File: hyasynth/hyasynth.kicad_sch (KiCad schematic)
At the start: 45 parts, among them J1 Conn_01x04_Male, J2 Conn_01x03_Male, J3 Conn_01x09_Male, J4 Conn_01x05_Male, J5 Conn_01x02_Male, SW1 Power Switch, SW10 G# Ab, SW11 A, SW12 A# Bb, SW13 B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

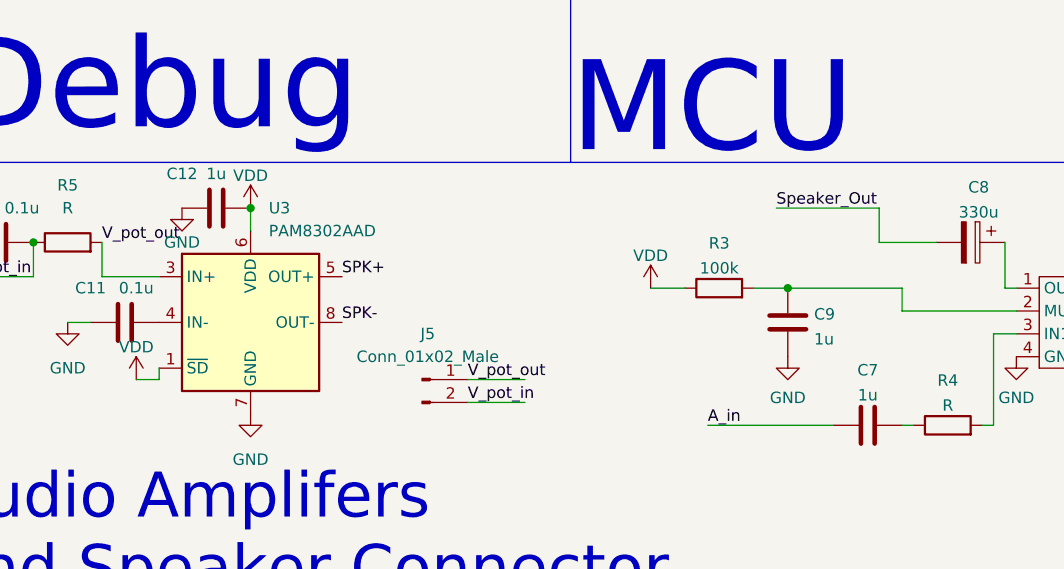
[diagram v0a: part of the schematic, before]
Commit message: set battery positions, adjusted for caps
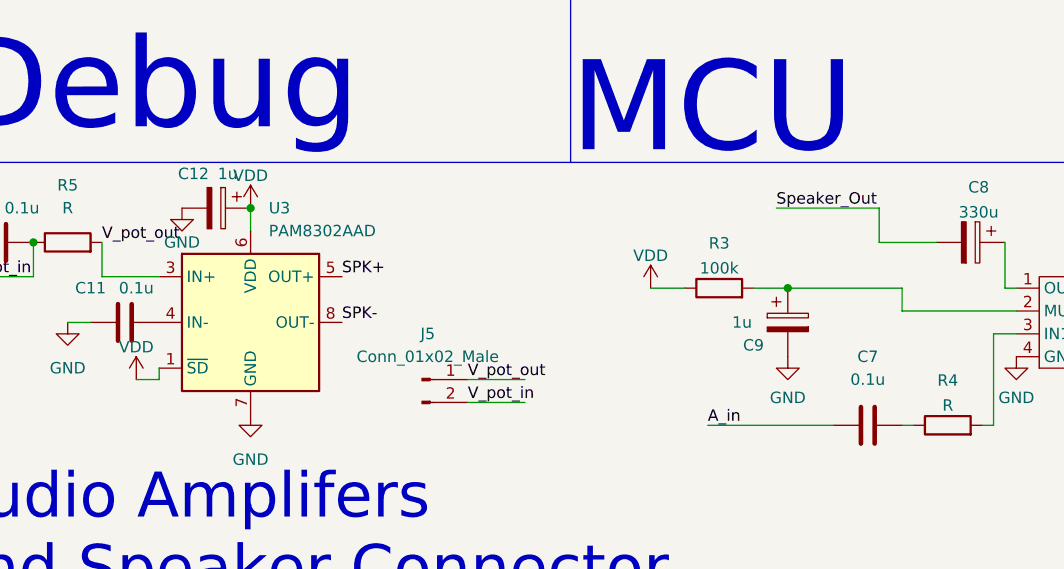
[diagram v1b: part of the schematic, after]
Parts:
- removed C12, C9: 1u, Capacitor_Tantalum_SMD:CP_EIA-3528-21_Kemet-B_Pad1.50x2.35mm_HandSolder, symbol Device:C
- added C12, C9: 1u, Capacitor_Tantalum_SMD:CP_EIA-3528-12_Kemet-T_Pad1.50x2.35mm_HandSolder, symbol Device:C_Polarized
- C7: value 1u -> 0.1u; footprint Capacitor_Tantalum_SMD:CP_EIA-3528-21_Kemet-B_Pad1.50x2.35mm_HandSolder -> Capacitor_SMD:C_0805_2012Metric_Pad1.18x1.45mm_HandSolder
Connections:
- net GND: now also C12.2, C9.2
- net VDD: now also C12.1
- net at R3.2, U2.2 (MUTE): now also C9.1
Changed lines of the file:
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@@
   (junction (at 38.1 175.26) (diameter 0) (color 0 0 0 0)
   )
+  (junction (at 175.26 97.79) (diameter 0) (color 0 0 0 0)
+  )
   (junction (at 267.97 158.75) (diameter 0) (color 0 0 0 0)
   )
+  (junction (at 212.09 49.53) (diameter 0) (color 0 0 0 0)
+  )
+  (junction (at 181.61 40.64) (diameter 0) (color 0 0 0 0)
+  )
+  (junction (at 181.61 36.83) (diameter 0) (color 0 0 0 0)
+  )
+  (junction (at 123.19 36.83) (diameter 0) (color 0 0 0 0)
+  )
+  (junction (at 86.36 185.42) (diameter 0) (color 0 0 0 0)
+  )
+  (junction (at 252.73 158.75) (diameter 0) (color 0 0 0 0)
+  )
+  (junction (at 215.9 44.45) (diameter 0) (color 0 0 0 0)
+  )
+  (junction (at 101.6 175.26) (diameter 0) (color 0 0 0 0)
+  )
+  (junction (at 158.75 40.64) (diameter 0) (color 0 0 0 0)
+  )
+  (junction (at 132.08 185.42) (diameter 0) (color 0 0 0 0)
+  )
+  (junction (at 158.75 29.21) (diameter 0) (color 0 0 0 0)
+  )
+  (junction (at 158.75 48.26) (diameter 0) (color 0 0 0 0)
+  )
+  (junction (at 69.85 175.26) (diameter 0) (color 0 0 0 0)
+  )
+  (junction (at 238.76 97.79) (diameter 0) (color 0 0 0 0)
+  )
+  (junction (at 91.44 92.71) (diameter 0) (color 0 0 0 0)
+  )
+  (junction (at 21.59 175.26) (diameter 0) (color 0 0 0 0)
+  )
+  (junction (at 215.9 49.53) (diameter 0) (color 0 0 0 0)
+  )
+  (junction (at 181.61 48.26) (diameter 0) (color 0 0 0 0)
+  )
+  (junction (at 101.6 185.42) (diameter 0) (color 0 0 0 0)
+  )
+  (junction (at 116.84 185.42) (diameter 0) (color 0 0 0 0)
+  )
+  (junction (at 54.61 185.42) (diameter 0) (color 0 0 0 0)
+  )
+  (junction (at 38.1 185.42) (diameter 0) (color 0 0 0 0)
+  )
+  (junction (at 86.36 175.26) (diameter 0) (color 0 0 0 0)
+  )
   (junction (at 115.57 88.9) (diameter 0) (color 0 0 0 0)
-  )
-  (junction (at 212.09 49.53) (diameter 0) (color 0 0 0 0)
-  )
-  (junction (at 181.61 40.64) (diameter 0) (color 0 0 0 0)
-  )
-  (junction (at 181.61 36.83) (diameter 0) (color 0 0 0 0)
-  )
-  (junction (at 123.19 36.83) (diameter 0) (color 0 0 0 0)
-  )
-  (junction (at 86.36 185.42) (diameter 0) (color 0 0 0 0)
-  )
-  (junction (at 252.73 158.75) (diameter 0) (color 0 0 0 0)
-  )
-  (junction (at 215.9 44.45) (diameter 0) (color 0 0 0 0)
-  )
-  (junction (at 101.6 175.26) (diameter 0) (color 0 0 0 0)
-  )
-  (junction (at 158.75 40.64) (diameter 0) (color 0 0 0 0)
-  )
-  (junction (at 132.08 185.42) (diameter 0) (color 0 0 0 0)
-  )
-  (junction (at 158.75 29.21) (diameter 0) (color 0 0 0 0)
-  )
-  (junction (at 158.75 48.26) (diameter 0) (color 0 0 0 0)
-  )
-  (junction (at 69.85 175.26) (diameter 0) (color 0 0 0 0)
-  )
-  (junction (at 238.76 97.79) (diameter 0) (color 0 0 0 0)
-  )
-  (junction (at 91.44 92.71) (diameter 0) (color 0 0 0 0)
-  )
-  (junction (at 21.59 175.26) (diameter 0) (color 0 0 0 0)
-  )
-  (junction (at 215.9 49.53) (diameter 0) (color 0 0 0 0)
-  )
-  (junction (at 181.61 48.26) (diameter 0) (color 0 0 0 0)
-  )
-  (junction (at 101.6 185.42) (diameter 0) (color 0 0 0 0)
-  )
-  (junction (at 175.26 97.79) (diameter 0) (color 0 0 0 0)
-  )
-  (junction (at 116.84 185.42) (diameter 0) (color 0 0 0 0)
-  )
-  (junction (at 54.61 185.42) (diameter 0) (color 0 0 0 0)
-  )
-  (junction (at 38.1 185.42) (diameter 0) (color 0 0 0 0)
-  )
-  (junction (at 86.36 175.26) (diameter 0) (color 0 0 0 0)
   )
   (no_connect (at 224.79 105.41))
@@
     (stroke (width 0) (type default) (color 0 0 0 0))
   )
-  (wire (pts (xy 187.96 97.79) (xy 175.26 97.79))
-    (stroke (width 0) (type default) (color 0 0 0 0))
-  )
   (wire (pts (xy 105.41 106.68) (xy 105.41 107.95))
     (stroke (width 0) (type default) (color 0 0 0 0))
@@
   )
   (wire (pts (xy 252.73 152.4) (xy 252.73 158.75))
+    (stroke (width 0) (type default) (color 0 0 0 0))
+  )
+  (wire (pts (xy 175.26 97.79) (xy 187.96 97.79))
     (stroke (width 0) (type default) (color 0 0 0 0))
   )
@@
     (pin "2")
   )
-  (symbol (lib_id "Device:C") (at 175.26 101.6 0) (unit 1)
-    (in_bom yes) (on_board yes) (fields_autoplaced)
-    (property "Reference" "C9" (id 0) (at 178.181 100.6915 0)
-      (effects (font (size 1.27 1.27)) (justify left))
-    )
-    (property "Value" "1u" (id 1) (at 178.181 103.4666 0)
-      (effects (font (size 1.27 1.27)) (justify left))
-    )
-    (property "Footprint" "Capacitor_Tantalum_SMD:CP_EIA-3528-21_Kemet-B_Pad1.50x2.35mm_HandSolder" (id 2) (at 176.2252 105.41 0)
-      (effects (font (size 1.27 1.27)) hide)
-    )
-    (property "Datasheet" "~" (id 3) (at 175.26 101.6 0)
-      (effects (font (size 1.27 1.27)) hide)
-    )
-    (pin "1")
-    (pin "2")
-  )
   (symbol (lib_id "power:VDD") (at 160.02 97.79 0) (unit 1)
     (in_bom yes) (on_board yes) (fields_autoplaced)
@@
     (pin "2")
   )
-  (symbol (lib_id "Device:C") (at 111.76 88.9 90) (unit 1)
-    (in_bom yes) (on_board yes)
-    (property "Reference" "C12" (id 0) (at 107.95 85.09 90))
-    (property "Value" "1u" (id 1) (at 111.76 85.09 90))
-    (property "Footprint" "Capacitor_Tantalum_SMD:CP_EIA-3528-21_Kemet-B_Pad1.50x2.35mm_HandSolder" (id 2) (at 115.57 87.9348 0)
-      (effects (font (size 1.27 1.27)) hide)
-    )
-    (property "Datasheet" "~" (id 3) (at 111.76 88.9 0)
-      (effects (font (size 1.27 1.27)) hide)
-    )
-    (pin "1")
-    (pin "2")
-  )
   (symbol (lib_id "power:GND") (at 31.75 57.15 0) (unit 1)
     (in_bom yes) (on_board yes)
@@
     )
     (property "Datasheet" "~" (id 3) (at 257.81 147.32 0)
+      (effects (font (size 1.27 1.27)) hide)
+    )
+    (pin "1")
+    (pin "2")
+  )
+  (symbol (lib_id "Device:C_Polarized") (at 111.76 88.9 270) (unit 1)
+    (in_bom yes) (on_board yes)
+    (property "Reference" "C12" (id 0) (at 109.22 85.09 90))
+    (property "Value" "1u" (id 1) (at 113.03 85.09 90))
+    (property "Footprint" "Capacitor_Tantalum_SMD:CP_EIA-3528-12_Kemet-T_Pad1.50x2.35mm_HandSolder" (id 2) (at 107.95 89.8652 0)
+      (effects (font (size 1.27 1.27)) hide)
+    )
+    (property "Datasheet" "~" (id 3) (at 111.76 88.9 0)
       (effects (font (size 1.27 1.27)) hide)
     )
@@
   (symbol (lib_id "Device:C") (at 184.15 113.03 90) (unit 1)
     (in_bom yes) (on_board yes) (fields_autoplaced)
-    (property "Reference" "C7" (id 0) (at 184.15 106.9045 90))
-    (property "Value" "1u" (id 1) (at 184.15 109.6796 90))
-    (property "Footprint" "Capacitor_Tantalum_SMD:CP_EIA-3528-21_Kemet-B_Pad1.50x2.35mm_HandSolder" (id 2) (at 187.96 112.0648 0)
+    (property "Reference" "C7" (id 0) (at 184.15 105.41 90))
+    (property "Value" "0.1u" (id 1) (at 184.15 107.95 90))
+    (property "Footprint" "Capacitor_SMD:C_0805_2012Metric_Pad1.18x1.45mm_HandSolder" (id 2) (at 187.96 112.0648 0)
       (effects (font (size 1.27 1.27)) hide)
     )
@@
     (pin "2")
   )
+  (symbol (lib_id "Device:C_Polarized") (at 175.26 101.6 0) (unit 1)
+    (in_bom yes) (on_board yes)
+    (property "Reference" "C9" (id 0) (at 171.45 104.14 0))
+    (property "Value" "1u" (id 1) (at 170.18 101.6 0))
+    (property "Footprint" "Capacitor_Tantalum_SMD:CP_EIA-3528-12_Kemet-T_Pad1.50x2.35mm_HandSolder" (id 2) (at 176.2252 105.41 0)
+      (effects (font (size 1.27 1.27)) hide)
+    )
+    (property "Datasheet" "~" (id 3) (at 175.26 101.6 0)
+      (effects (font (size 1.27 1.27)) hide)
+    )
+    (pin "1")
+    (pin "2")
+  )
   (symbol (lib_id "power:GND") (at 208.28 50.8 0) (unit 1)
     (in_bom yes) (on_board yes) (fields_autoplaced)
@@
     )
     (path "/513f0865-9379-4edb-99ef-467c198a4fc2"
-      (reference "C7") (unit 1) (value "1u") (footprint "Capacitor_Tantalum_SMD:CP_EIA-3528-21_Kemet-B_Pad1.50x2.35mm_HandSolder")
+      (reference "C7") (unit 1) (value "0.1u") (footprint "Capacitor_SMD:C_0805_2012Metric_Pad1.18x1.45mm_HandSolder")
     )
     (path "/fb89f98f-00cc-4cff-9de7-c39abf7310f9"
       (reference "C8") (unit 1) (value "330u") (footprint "Capacitor_THT:CP_Radial_D8.0mm_P3.50mm")
     )
-    (path "/10707312-5bbe-4424-819e-e8b88fb18d88"
-      (reference "C9") (unit 1) (value "1u") (footprint "Capacitor_Tantalum_SMD:CP_EIA-3528-21_Kemet-B_Pad1.50x2.35mm_HandSolder")
+    (path "/c64a49e3-a6e3-4ae6-b140-03aa621e9e81"
+      (reference "C9") (unit 1) (value "1u") (footprint "Capacitor_Tantalum_SMD:CP_EIA-3528-12_Kemet-T_Pad1.50x2.35mm_HandSolder")
     )
     (path "/b7a6bb1f-8fe6-40d7-91b8-592d0ab889d4"
@@
       (reference "C11") (unit 1) (value "0.1u") (footprint "Capacitor_SMD:C_0805_2012Metric_Pad1.18x1.45mm_HandSolder")
     )
-    (path "/2b0caee0-ca6a-43b8-9f33-83168c92cb30"
-      (reference "C12") (unit 1) (value "1u") (footprint "Capacitor_Tantalum_SMD:CP_EIA-3528-21_Kemet-B_Pad1.50x2.35mm_HandSolder")
+    (path "/3212fb31-6c72-4476-a39a-a9c0b82ecb0b"
+      (reference "C12") (unit 1) (value "1u") (footprint "Capacitor_Tantalum_SMD:CP_EIA-3528-12_Kemet-T_Pad1.50x2.35mm_HandSolder")
     )
     (path "/748a6a47-fa8d-4129-923b-a3e1d8211e5e"

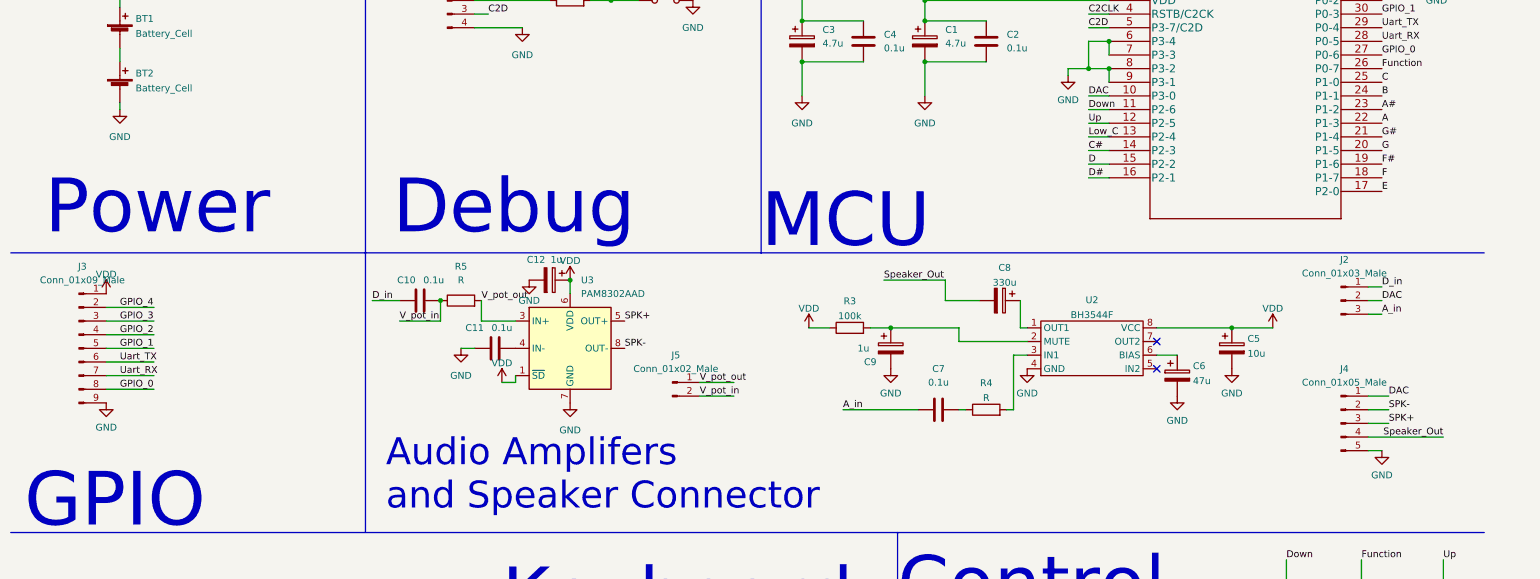
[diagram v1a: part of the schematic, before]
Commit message: laid out switches, started routing them.
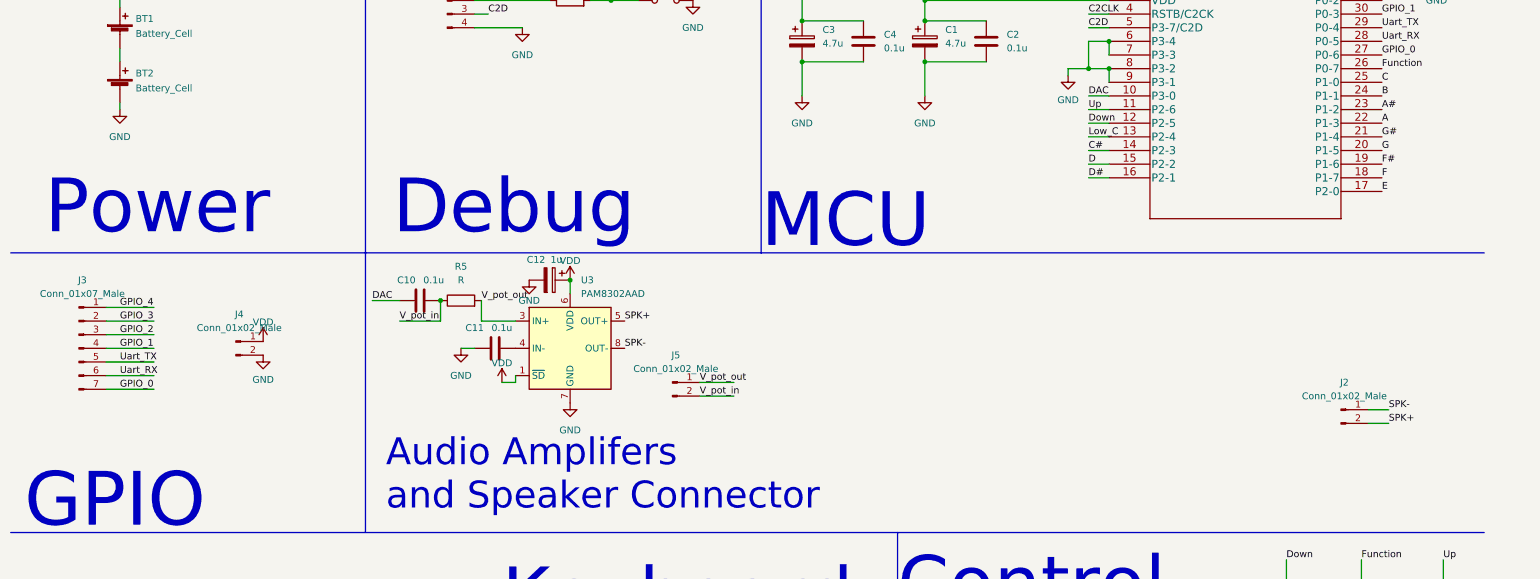
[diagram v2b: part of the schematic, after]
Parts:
- removed C5: 10u, Capacitor_Tantalum_SMD:CP_EIA-7343-31_Kemet-D_Pad2.25x2.55mm_HandSolder, symbol Device:C_Polarized
- removed C6: 47u, Capacitor_THT:CP_Radial_D8.0mm_P3.50mm, symbol Device:C_Polarized
- removed C7: 0.1u, Capacitor_SMD:C_0805_2012Metric_Pad1.18x1.45mm_HandSolder, symbol Device:C
- removed C8: 330u, Capacitor_THT:CP_Radial_D8.0mm_P3.50mm, symbol Device:C_Polarized
- removed C9: 1u, Capacitor_Tantalum_SMD:CP_EIA-3528-12_Kemet-T_Pad1.50x2.35mm_HandSolder, symbol Device:C_Polarized
- removed J2: Conn_01x03_Male, Connector_PinHeader_2.54mm:PinHeader_1x03_P2.54mm_Vertical, symbol Connector:Conn_01x03_Male
- removed J3: Conn_01x09_Male, Connector_PinHeader_2.54mm:PinHeader_1x09_P2.54mm_Vertical, symbol Connector:Conn_01x09_Male
- removed J4: Conn_01x05_Male, Connector_PinHeader_2.54mm:PinHeader_1x05_P2.54mm_Vertical, symbol Connector:Conn_01x05_Male
- removed R3: 100k, Resistor_SMD:R_0805_2012Metric_Pad1.20x1.40mm_HandSolder, symbol Device:R
- removed R4: R, Resistor_SMD:R_0805_2012Metric_Pad1.20x1.40mm_HandSolder, symbol Device:R
- removed U2: BH3544F, Package_SO:SOP-8_3.76x4.96mm_P1.27mm, symbol BH3544F:BH3544F
- added J2, J4: Conn_01x02_Male, Connector_PinHeader_2.54mm:PinHeader_1x02_P2.54mm_Vertical, symbol Connector:Conn_01x02_Male
- added J3: Conn_01x07_Male, Connector_PinHeader_2.54mm:PinHeader_1x07_P2.54mm_Vertical, symbol Connector:Conn_01x07_Male
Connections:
- net D_in is gone; now on net DAC: C10.1
- net Down: now also U1.12 (P2-5); no longer U1.11 (P2-6)
- net GND: now also J4.2 (Pin_2)
- net GPIO_0: now also J3.7 (Pin_7)
- net GPIO_1: now also J3.4 (Pin_4)
- net GPIO_2: now also J3.3 (Pin_3)
- net GPIO_3: now also J3.2 (Pin_2)
- net GPIO_4: now also J3.1 (Pin_1)
- net SPK+: now also J2.2 (Pin_2)
- net SPK-: now also J2.1 (Pin_1)
- net Uart_RX: now also J3.6 (Pin_6)
- net Uart_TX: now also J3.5 (Pin_5)
- net Up: now also U1.11 (P2-6); no longer U1.12 (P2-5)
- net VDD: now also J4.1 (Pin_1)
- no-connect marks 2 -> 0
